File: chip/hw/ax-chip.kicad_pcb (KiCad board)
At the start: 2 copper layers, 41 x 60.5 mm, 73 parts, among them IC1 CHIPv1_0, IC2 TPS73433, IC3 AX5043, IC4 TG-5006CJ, J1 CONN_01x02, J2 CONN_01x02, P1 PAD, P2 COAX, P3 COAX, P5 PAD, Q1 NX7002AK, U1 DS2401P

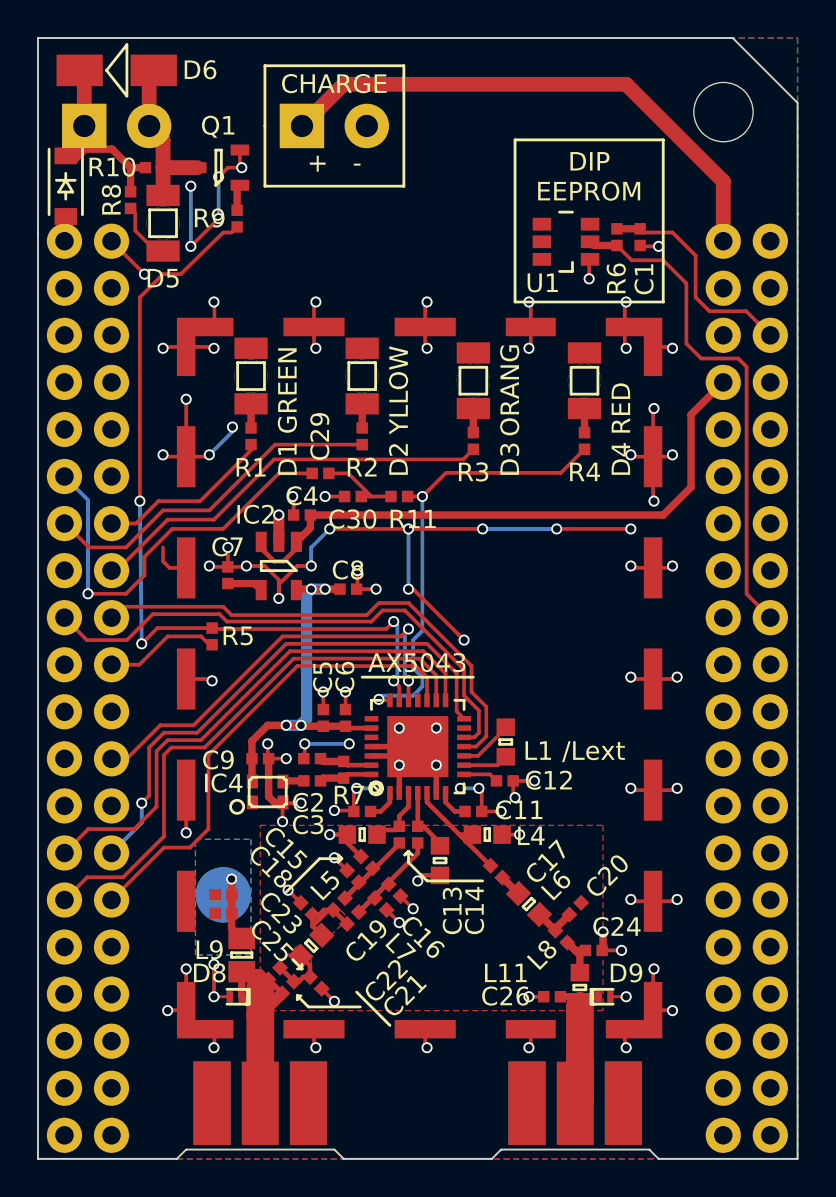
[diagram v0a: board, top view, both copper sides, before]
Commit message: [chip hw] add LNA, remove dc power inject
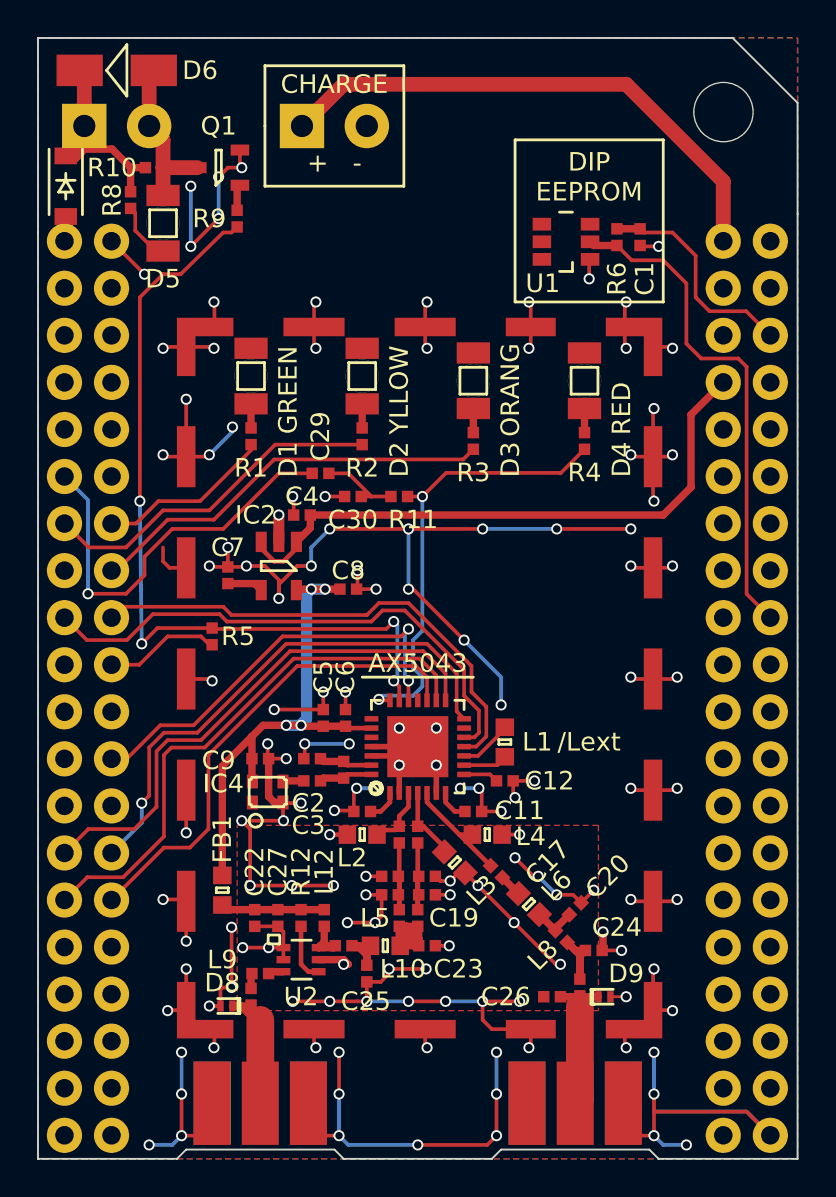
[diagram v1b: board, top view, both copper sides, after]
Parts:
- removed P5: PAD, agg:WIREPAD
- added FB1: 600Ω-1A-0.2DCR, agg:0603, F.Cu at (210.9, 134.5)
- added L12: 47nH, agg:0402, F.Cu at (216.4, 136.0)
- added R12: 1kΩ, agg:0402, F.Cu at (215.2, 136.0)
- added U2: MGA-62563, TO_SOT_Packages_SMD:SC-70-6, F.Cu at (215.2, 138.2)
- C21, C28: value 1nF -> 10nF
- C22: value 100pF -> 10nF
- C27: value 100nF -> 68pF
- L11: footprint agg:0603 -> agg:0402
- L9: value 2.2µH -> 6.8nH; footprint agg:0805 -> agg:0402
- moved C28 7.06 mm to (217.5, 137.5), turned to 0 degrees
- moved C23 6.80 mm to (222.0, 137.5), turned to 0 degrees
- moved L10 4.00 mm to (219.8, 137.5), turned to 180 degrees
- moved C19 3.50 mm to (221.5, 136.0), turned to 90 degrees
- moved L5 3.34 mm to (220.5, 136.0), turned to 90 degrees
- moved C22 3.18 mm to (212.7, 136.0), turned to 270 degrees
- moved C27 2.96 mm to (213.9, 136.0), turned to 270 degrees
- moved C25 2.80 mm to (218.8, 139.0), turned to 270 degrees
- moved L7 2.55 mm to (222.0, 134.8), turned to 0 degrees
- moved C18 2.24 mm to (220.0, 134.8), turned to 180 degrees
- moved C21 2.06 mm to (212.5, 140.2), turned to 90 degrees
- moved C16 1.90 mm to (222.0, 133.8), turned to 0 degrees
- moved C15 1.46 mm to (220.0, 133.8), turned to 0 degrees
- moved L9 1.41 mm to (213.0, 139.0), turned to 0 degrees
- moved L3 0.81 mm to (223.5, 133.0), turned to 315 degrees
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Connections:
- C21 pad 1: AX_50Ω_DIFF -> /AX_ANT_DIFF
- C21 pad 2: /AX_ANT_DIFF -> Net-(C21-Pad2)
- C22 pad 1: AX_50Ω_DIFF -> /V_LNA
- C22 pad 2: /AX_ANT_DIFF -> GND
- C27 pad 1: /DC -> /V_LNA
- C28 pad 1: /DC -> /LNA_OUT
- C28 pad 2: GND -> AX_50Ω_DIFF
- L9 pad 1: /DC -> Net-(C21-Pad2)
- L9 pad 2: /AX_ANT_DIFF -> Net-(L9-Pad2)
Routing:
- net GND: track 169.9 -> 288.2 mm, vias 98 -> 141
- net VDD: track 20.6 -> 28.9 mm
- net /V_LNA: track 0.00 -> 5.60 mm
- net /AX_ANT_DIFF: track 13.4 -> 8.59 mm
- net /DC: track 4.46 -> 0.00 mm, vias 1 -> 0
- net Net-(C19-Pad1): track 5.07 -> 8.47 mm
- net /LNA_OUT: track 0.00 -> 3.37 mm
- net Net-(R12-Pad2): track 0.00 -> 3.17 mm
- net Net-(C14-Pad2): track 7.35 -> 5.46 mm
- net Net-(C24-Pad1): track 3.07 -> 4.75 mm
- net Net-(C13-Pad2): track 6.50 -> 5.51 mm
- net Net-(L9-Pad2): track 0.00 -> 0.84 mm
- net Net-(C21-Pad2): track 0.00 -> 0.82 mm
- removed copper zone on F.Cu, net /AX_ANT_DIFF
- removed copper zone on B.Cu, net /DC
- removed copper zone on F.Cu, net AX_50Ω_DIFF
- removed copper zone on F.Cu, net Net-(C19-Pad1)
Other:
- board text added: "charge/charger /питание"
- board text added: "optional/optionnel/необязательный LNA Малошумящий усилитель"
- board text added: "receive/récepteur/радиоприемник 70 cm/cm/см and/et/и 2 meters/mètres/метрa"
- board text added: "transmit/émettre/передатчик 2 meters/mètres/метрa"
- board text removed: "charge/charger /заряд"
- board text removed: "optional/optionnel/необязательный LNA"
- board text removed: "receive/récepteur/радиоприемник 70 cm/cm/см and/et/и 2 meters/mètres/метры"
- board text removed: "transmit/émettre/транслировать 2 meters/mètres/метры"
